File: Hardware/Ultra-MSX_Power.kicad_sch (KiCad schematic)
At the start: 42 parts, among them J1 Conn_KLDX-0202-A, J10 Molex_0469990346, U1 MPU_Z380, U10 SST39SF040, U14 D41464, U15 D41464, U16 D41464, U17 D41464, U3 V9958, U4 YM2610, U5 BQ4802YPW, U6 LMH1980, U8 AS6C4008-55STIN, U9 DAC_YM3016

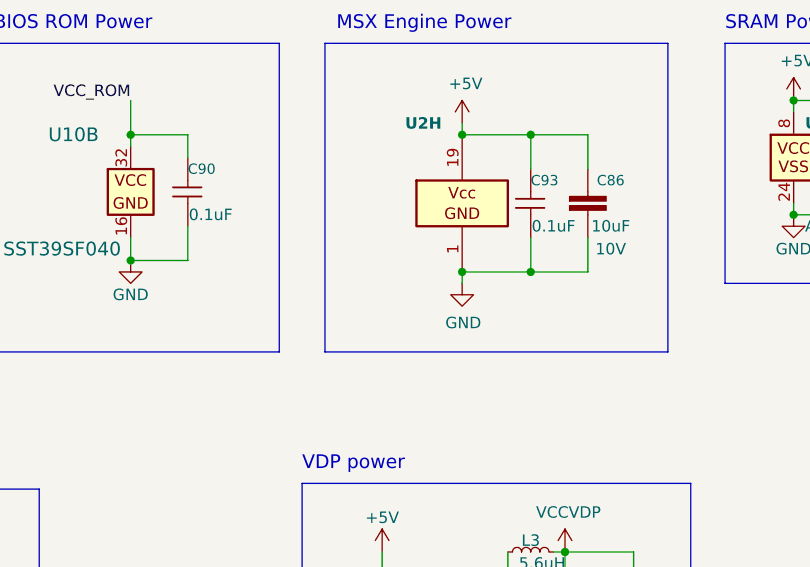
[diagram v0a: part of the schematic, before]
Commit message: Routed the VDP-board further, as well as making it a 4-layer board - also added an exception in the gitignore, for big images.
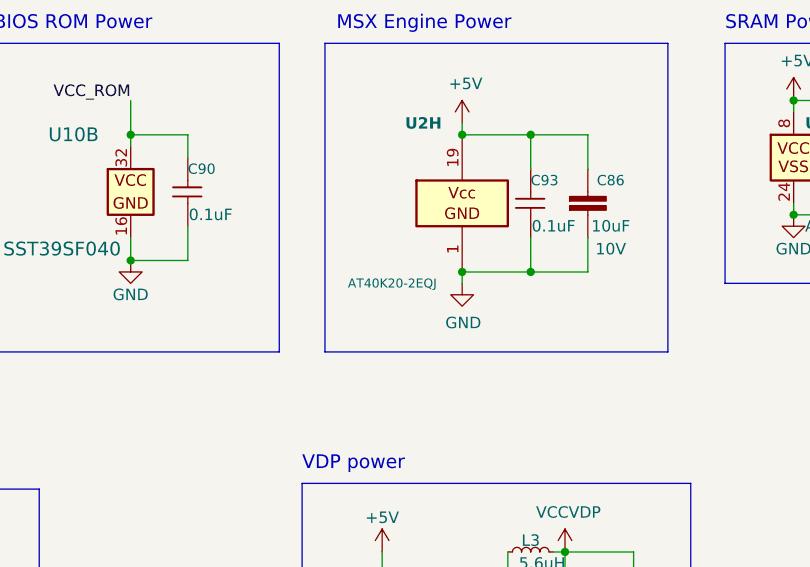
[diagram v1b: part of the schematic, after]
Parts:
- U2: value (none) -> AT40K20-2EQJ; footprint (none) -> Package_QFP:PQFP-240_32.1x32.1mm_P0.5mm
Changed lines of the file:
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@@
       (effects (font (size 1.27 1.27) bold) (justify left))
     )
-    (property "Value" "" (id 1) (at 243.84 53.34 0)
+    (property "Value" "AT40K20-2EQJ" (id 1) (at 243.84 53.34 0)
       (effects (font (size 1 1)) (justify left))
     )
-    (property "Footprint" "" (id 2) (at 290.83 21.59 0)
+    (property "Footprint" "Package_QFP:PQFP-240_32.1x32.1mm_P0.5mm" (id 2) (at 290.83 21.59 0)
       (effects (font (size 1.27 1.27)) (justify left) hide)
     )

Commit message: Finished the VDP-board, finished up the mixer-section, removed the buffer-pins from the FPGA, and instead added external buffers for the slots, designed a marquee-block with the Ultra-MSX logo, designed the logotype, andmultiple other changes.
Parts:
- removed C73, C89: C_GRM21BR71A106KA73K, Capacitor_SMD:C_0805_2012Metric_Pad1.18x1.45mm_HandSolder, symbol LRJ-parts:C_GRM21BR71A106KA73K
- removed C77, C91, C92: C_CC0805JPX7R9BB104, Capacitor_SMD:C_0805_2012Metric, symbol LRJ-parts:C_CC0805JPX7R9BB104
- removed U14, U15, U16, U17: D41464, Ultra-MSX:IC_DIP18_300, symbol Ultra-MSX:D41464
- removed U3: V9958, Ultra-MSX:IC_SDIP64_600, symbol Ultra-MSX:V9958
- removed U6: LMH1980, Package_SO:VSSOP-10_3x3mm_P0.5mm, symbol LRJ-parts:LMH1980
- added C1, C10, C13, C3, C36, C41, C5, C6, C74, C9: C_CC0805JPX7R9BB104, Capacitor_SMD:C_0805_2012Metric, symbol LRJ-parts:C_CC0805JPX7R9BB104
- added C11, C12, C2, C37, C4, C66, C67, C7, C75, C8: C_GRM21BR71A106KA73K, Capacitor_SMD:C_0805_2012Metric_Pad1.18x1.45mm_HandSolder, symbol LRJ-parts:C_GRM21BR71A106KA73K
- added C68, C69: C_GRM32EC81C476KE15K, Capacitor_SMD:C_1210_3225Metric, symbol LRJ-parts:C_GRM32EC81C476KE15K
- added RV1: CAT5140ZI-50, Package_SO:TSSOP-8_3x3mm_P0.65mm, symbol LRJ-parts:CAT5140ZI-50
- added RV4, RV8: AD5144ABRUZ100, Package_SO:TSSOP-20_4.4x6.5mm_P0.65mm, symbol LRJ-parts:AD5144ABRUZ100
- added RV5, RV6: MCP4461, Package_SO:TSSOP-20_4.4x6.5mm_P0.65mm, symbol LRJ-parts:MCP4461
- added U14: SN74ABTH16244DL, Package_SO:TSSOP-56_6.1x14mm_P0.5mm, symbol LRJ-parts:SN74ABTH16244DL
- added U15: SN74ABT241APW, Package_SO:TSSOP-56_6.1x14mm_P0.5mm, symbol LRJ-parts:SN74ABT241APW
- added U6: 74ABT245PW_118, Package_SO:TSSOP-20_4.4x6.5mm_P0.65mm, symbol LRJ-parts:74ABT245PW_118
- added virt_sym1: Virtual_symbol, LRJ:TestPoint_Bridge_Pitch1.5mm_Pad0.8mm, symbol LRJ-parts:Virtual_symbol
- renumbered C17 to C20, J10 to J10-0, J1 to J10-1
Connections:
- net +12V: now also L2.1
- net +5V: now also C1.1, C10.1, C11.1, C12.1, C2.1, C3.1, C4.1, C68.2, C69.2, C74.1, C75.1, C9.1, RV4.17 (V_{LOGIC}), RV8.17 (V_{LOGIC}), U14.18 (VCC), U14.31 (VCC), U14.42 (VCC), U14.7 (VCC), U15.20 (VCC), U6.20 (VCC); no longer L2.1, L3.1
- net +5VSB: now also virt_sym1.1
- net -12V: now also L3.1
- net GND: now also C1.2, C10.2, C11.2, C12.2, C2.2, C3.2, C4.2, C74.2, C75.2, C9.2, RV4.2 (GND), RV8.2 (GND), U14.10 (GND), U14.15 (GND), U14.21 (GND), U14.28 (GND), U14.34 (GND), U14.39 (GND), U14.4 (GND), U14.45 (GND), U15.10 (GND), U6.10 (GND); no longer C28.2, C30.2, C32.1, C33.1, C34.1, C39.1, J10-0.15 (GND), J10-0.17 (GND), J10-0.18 (GND), J10-0.19 (GND), J10-0.24 (GND), J10-0.3 (GND), J10-0.5 (GND), J10-0.7 (GND), J10-1.2, J10-1.3
- net GNDA: now also C13.2, C36.2, C37.2, C41.2, C5.2, C6.2, C66.2, C67.2, C7.2, C8.2, RV1.4 (GND), RV4.9 (V_{SS}), RV5.7 (V_{SS}), RV6.7 (V_{SS}), RV8.9 (V_{SS})
- net VCCRGB: no longer L2.2
- net VCCVDP: no longer L3.2
- net VCC_DAC: now also C13.1, C36.1, C37.1, C41.1, C5.1, C6.1, C66.1, C67.1, C7.1, C8.1, RV1.8 (V_{CC}), RV4.16 (V_{DD}), RV5.17 (V_{DD}), RV6.17 (V_{DD}), RV8.16 (V_{DD})
- net at U1.42 (~{STNBY}): now also virt_sym1.1
- new net +12VA: L2.2
- new net -12VA: L3.2
- new net GNDPWR1: C28.2, C30.2, C32.1, C33.1, C34.1, C39.1, J10-0.15 (GND), J10-0.17 (GND), J10-0.18 (GND), J10-0.19 (GND), J10-0.24 (GND), J10-0.3 (GND), J10-0.5 (GND), J10-0.7 (GND)
- new net GNDPWR2: C68.1, C69.1, J10-1.2, J10-1.3
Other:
- note added: "ATX connector"
- note added: "Barreljack Backup"
- note added: "Digital Potentiometer power"
- note added: "Filtering for analogue components"
- note added: "Power-management: ---- https://www.embedded.com/adding-a-power-management-mcu-to-your-system-reduces-standby-energy-use/ -- MAKE A STAR-GROUND-CONNECTION!"
- note added: "Primary Power input"
- note added: "Slot Buffer Power"
- note removed: "Power-management: ---- https://www.embedded.com/adding-a-power-management-mcu-to-your-system-reduces-standby-energy-use/"
- note removed: "Primary Power input (ATX)"
- note removed: "Sync Separator power"
- note removed: "VDP power"
- note removed: "VRAM Power"
- note removed: "https://powersupply33.com/atx-power-supply-pinout.html https://pinouts.ru/Power/atx_v2_pinout.shtml"
- moved on the sheet: C15, C16, C22, C28, C30, C32, C33, C34, C39, C59, C63, C86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

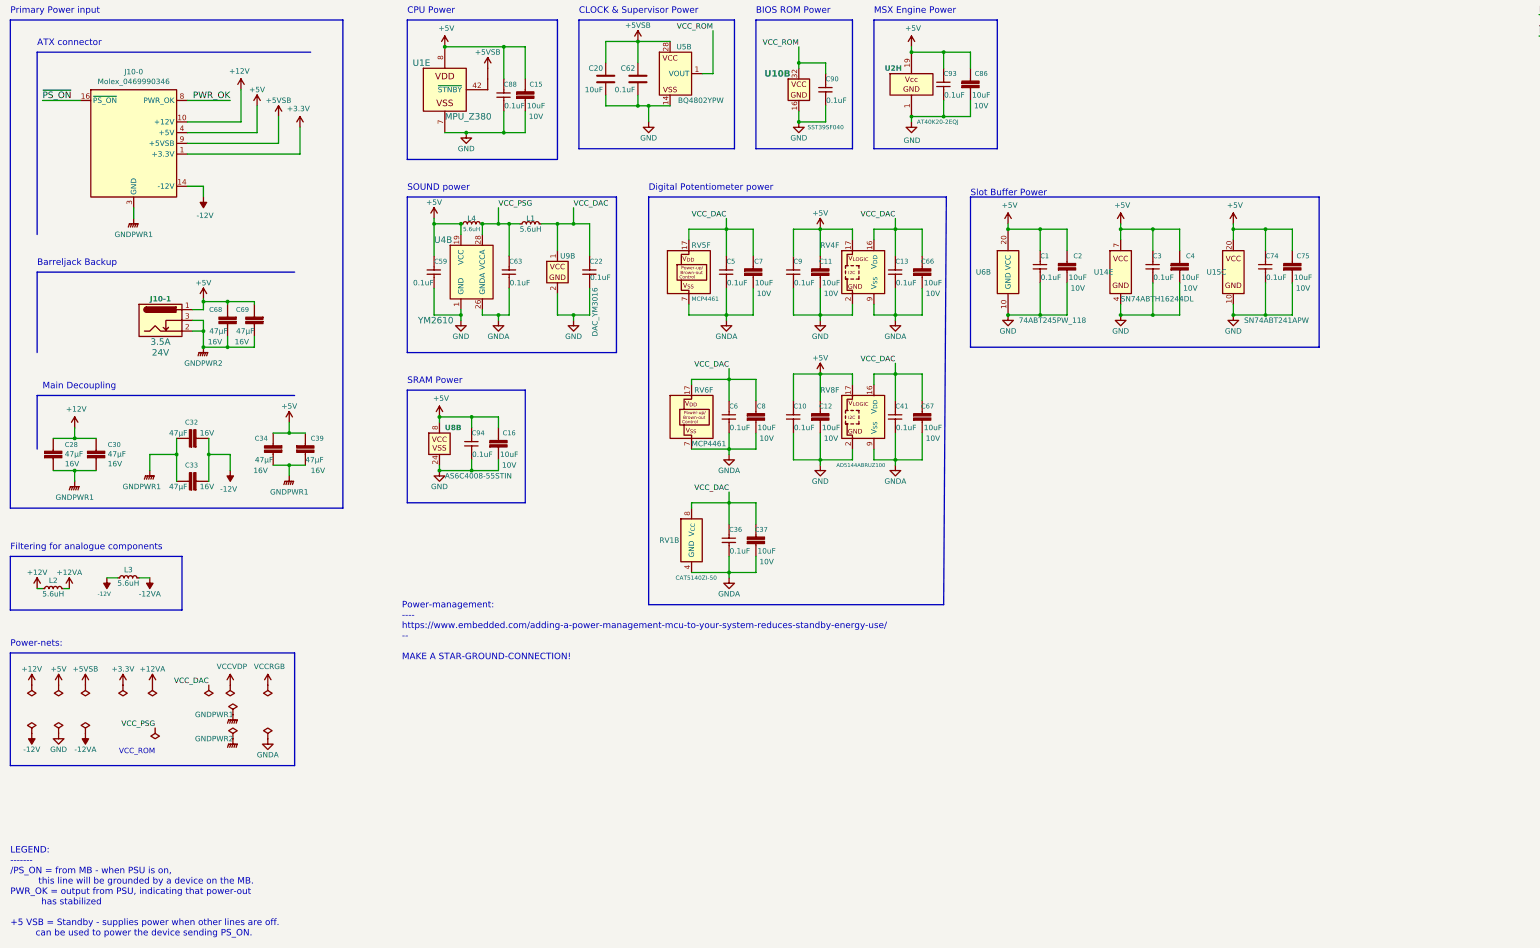
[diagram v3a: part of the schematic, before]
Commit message: Added SD-card slot, made basic 3d-model for sd-card slot, connected it up in the schematic, and numerous other tweaks.
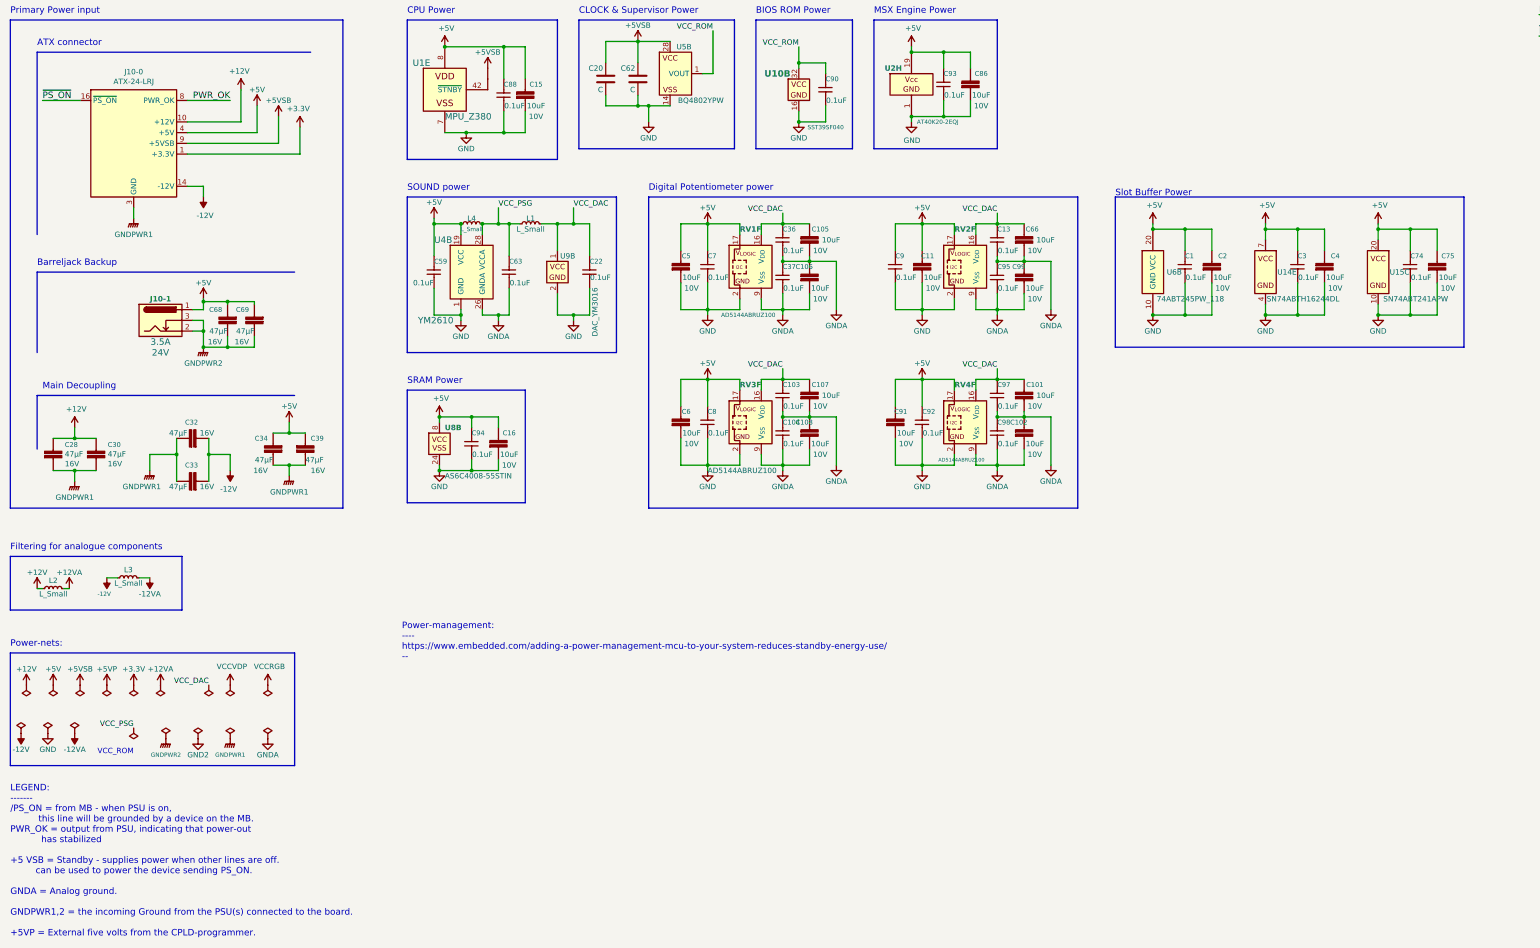
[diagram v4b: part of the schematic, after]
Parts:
- removed C10, C41, C5, C6: C_CC0805JPX7R9BB104, Capacitor_SMD:C_0805_2012Metric, symbol LRJ-parts:C_CC0805JPX7R9BB104
- removed C12, C37, C67, C7, C8: C_GRM21BR71A106KA73K, Capacitor_SMD:C_0805_2012Metric_Pad1.18x1.45mm_HandSolder, symbol LRJ-parts:C_GRM21BR71A106KA73K
- removed RV1: CAT5140ZI-50, Package_SO:TSSOP-8_3x3mm_P0.65mm, symbol LRJ-parts:CAT5140ZI-50
- removed RV8: AD5144ABRUZ100, Package_SO:TSSOP-20_4.4x6.5mm_P0.65mm, symbol LRJ-parts:AD5144ABRUZ100
- added C101, C102, C105, C106, C107, C108, C5, C6, C91, C99: C_GRM21BR71A106KA73K, Capacitor_SMD:C_0805_2012Metric_Pad1.18x1.45mm_HandSolder, symbol LRJ-parts:C_GRM21BR71A106KA73K
- added C103, C104, C37, C7, C8, C92, C95, C97, C98: C_CC0805JPX7R9BB104, Capacitor_SMD:C_0805_2012Metric, symbol LRJ-parts:C_CC0805JPX7R9BB104
- added RV4: AD5144ABRUZ100, Package_SO:TSSOP-20_4.4x6.5mm_P0.65mm, symbol LRJ-parts:AD5144ABRUZ100
- C20: value 10uF -> C
- C62: value 0.1uF -> C
- J10-0: value Molex_0469990346 -> ATX-24-LRJ
- L1, L2, L3, L4: value 5.6uH -> L_Small
- RV1: renamed from RV5; value MCP4461 -> AD5144ABRUZ100; symbol LRJ-parts:MCP4461 -> LRJ-parts:AD5144ABRUZ100; MPN MCP4461-503E/ST -> AD5144ABRUZ100; Manufacturer Microchip Technology -> Analog Devices Inc.; Tolerance (none) -> ±8%
- RV2: renamed from RV4; Tolerance (none) -> ±8%
- RV3: renamed from RV6; value MCP4461 -> AD5144ABRUZ100; symbol LRJ-parts:MCP4461 -> LRJ-parts:AD5144ABRUZ100; MPN MCP4461-503E/ST -> AD5144ABRUZ100; Manufacturer Microchip Technology -> Analog Devices Inc.; Tolerance (none) -> ±8%
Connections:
- net +5V: now also RV1.17 (V_{LOGIC}), RV3.17 (V_{LOGIC}), C5.1, C6.1, C7.1, C8.1, C91.1, C92.1, RV4.17 (V_{LOGIC})
- net GND: now also RV1.2 (GND), RV3.2 (GND), C5.2, C6.2, C7.2, C8.2, C91.2, C92.2, RV4.2 (GND)
- net GNDA: now also RV1.9 (V_{SS}), RV3.9 (V_{SS}), C101.2, C102.1, C102.2, C103.2, C104.1, C104.2, C105.2, C106.1, C106.2, C107.2, C108.1, C108.2, C37.1, C37.2, C95.1, C95.2, C97.2, C98.1, C98.2, C99.1, C99.2, RV4.9 (V_{SS}); no longer RV1.7 (V_{SS}), RV3.7 (V_{SS})
- net VCC_DAC: now also RV1.16 (V_{DD}), RV3.16 (V_{DD}), C101.1, C103.1, C105.1, C107.1, C97.1, RV4.16 (V_{DD}); no longer RV1.17 (V_{DD}), RV3.17 (V_{DD})
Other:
- note added: "LEGEND: ------- /PS_ON = from MB - when PSU is on, this line will be grounded by a device on the MB. PWR_OK = output from PSU, indicating that power-out has stabilized +5 VSB = Standby - supplies power when other lines are off. can be used to power the device sending PS_ON. GNDA = Analog ground. GNDPWR1,2 = the incoming Ground from the PSU(s) connected to the board. +5VP = External five volts fro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"
- note added: "Power-management: ---- https://www.embedded.com/adding-a-power-management-mcu-to-your-system-reduces-standby-energy-use/ --"
- note removed: "LEGEND: ------- /PS_ON = from MB - when PSU is on, this line will be grounded by a device on the MB. PWR_OK = output from PSU, indicating that power-out has stabilized +5 VSB = Standby - supplies power when other lines are off. can be used to power the device sending PS_ON."
- note removed: "Power-management: ---- https://www.embedded.com/adding-a-power-management-mcu-to-your-system-reduces-standby-energy-use/ -- MAKE A STAR-GROUND-CONNECTION!"
- moved on the sheet: C1, C11, C13, C2, C3, C4, C66, C74, C75, C9, RV2F

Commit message: Redesigned VDP-board to include a socket, increased it to 4 layers. Various clean-ups here and there. Improved the printer-port and joystick-port 3D-models. Improved the cooling-fin 3D-model, and added attachment-spring in 3D-model.
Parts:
- U14: footprint Package_SO:TSSOP-56_6.1x14mm_P0.5mm -> LRJ:Texas_R-PDSO-G48_7.7x16.0mm
- U15: footprint Package_SO:TSSOP-56_6.1x14mm_P0.5mm -> Package_SO:Texas_PWP0020A; MPN SN74ABTH16244DL -> SN74ABT241APW
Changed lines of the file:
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@@
     (property "Reference" "U15" (id 0) (at 347.98 85.09 0))
     (property "Value" "SN74ABT241APW" (id 1) (at 351.79 91.44 0))
-    (property "Footprint" "Package_SO:TSSOP-56_6.1x14mm_P0.5mm" (id 2) (at 304.8 77.47 0)
+    (property "Footprint" "Package_SO:Texas_PWP0020A" (id 2) (at 304.8 77.47 0)
       (effects (font (size 1.27 1.27)) hide)
     )
@@
       (effects (font (size 1.27 1.27)) hide)
     )
-    (property "MPN" "SN74ABTH16244DL" (id 5) (at 314.96 67.31 0)
-      (effects (font (size 1.27 1.27)) hide)
-    )
-    (property "Description" "BUF NON-INVERT 5.5V 48SSOP" (id 6) (at 309.88 72.39 0)
+    (property "MPN" "SN74ABT241APW" (id 5) (at 314.96 67.31 0)
+      (effects (font (size 1.27 1.27)) hide)
+    )
+    (property "Description" "BUF NON-INVERT 5.5V 20-TSSOP" (id 6) (at 309.88 72.39 0)
       (effects (font (size 1.27 1.27)) hide)
     )
@@
     (property "Reference" "U14" (id 0) (at 321.31 85.09 0))
     (property "Value" "SN74ABTH16244DL" (id 1) (at 325.12 91.44 0))
-    (property "Footprint" "Package_SO:TSSOP-56_6.1x14mm_P0.5mm" (id 2) (at 278.13 77.47 0)
-      (effects (font (size 1.27 1.27)) hide)
-    )
+    (property "Footprint" "LRJ:Texas_R-PDSO-G48_7.7x16.0mm" (id 2) (at 278.13 77.47 0)
+      (effects (font (size 1.27 1.27)) hide)
+    )

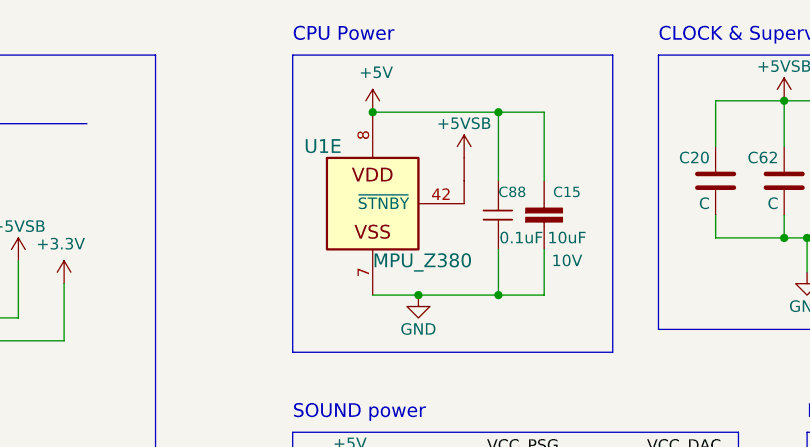
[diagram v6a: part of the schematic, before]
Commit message: Reworked the Printer-port 3D model, and the Scart 3D-model. Generated a 3D model of the main board. Moved peripheral components from separate expansion-headers, to a singular IO-shield board.
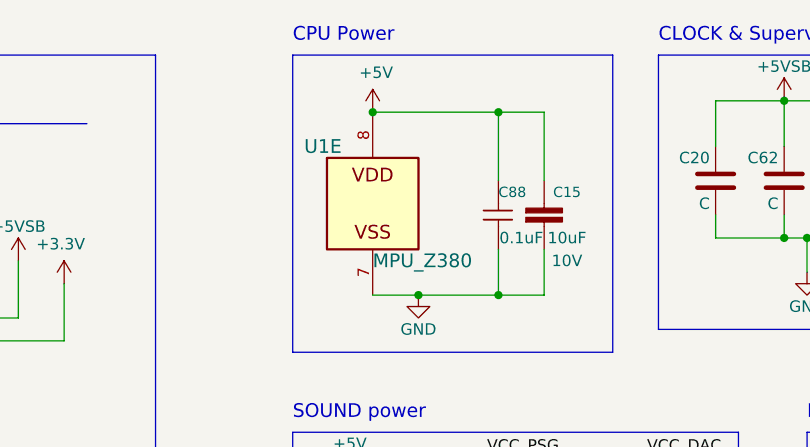
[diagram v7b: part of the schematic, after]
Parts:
- removed virt_sym1: Virtual_symbol, LRJ:TestPoint_Bridge_Pitch1.5mm_Pad0.8mm, symbol LRJ-parts:Virtual_symbol
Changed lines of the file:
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@@
     (pin "40")
     (pin "41")
+    (pin "42")
     (pin "43")
     (pin "11")
@@
     (pin "29")
     (pin "30")
-    (pin "42")
     (pin "50")
     (pin "51")
@@
     (pin "2")
   )
-  (symbol (lib_id "LRJ-parts:Virtual_symbol") (at 132.08 39.37 0) (unit 1)
-    (in_bom no) (on_board no) (fields_autoplaced)
-    (property "Reference" "virt_sym1" (id 0) (at 137.16 36.83 0)
-      (effects (font (size 1.27 1.27)) hide)
-    )
-    (property "Value" "Virtual_symbol" (id 1) (at 139.7 39.37 0)
-      (effects (font (size 1.27 1.27)) hide)
-    )
-    (property "Footprint" "LRJ:TestPoint_Bridge_Pitch1.5mm_Pad0.8mm" (id 2) (at 132.715 48.26 0)
-      (effects (font (size 1.27 1.27)) hide)
-    )
-    (property "Datasheet" "" (id 3) (at 134.62 36.83 0)
-      (effects (font (size 1.27 1.27)) hide)
-    )
-    (pin "1")
-    (pin "1")
-  )
   (symbol (lib_id "power:GND") (at 289.56 95.25 0) (unit 1)
     (in_bom yes) (on_board yes)
@@
     (pin "7")
   )
-  (symbol (lib_id "LRJ-parts:+5VSB") (at 132.08 36.83 0) (unit 1)
-    (in_bom no) (on_board yes)
-    (property "Reference" "#PWR034" (id 0) (at 132.08 40.64 0)
-      (effects (font (size 1.27 1.27)) hide)
-    )
-    (property "Value" "+5VSB" (id 1) (at 132.08 33.02 0))
-    (property "Footprint" "" (id 2) (at 132.08 36.83 0)
-      (effects (font (size 1.27 1.27)) hide)
-    )
-    (property "Datasheet" "" (id 3) (at 132.08 36.83 0)
-      (effects (font (size 1.27 1.27)) hide)
-    )
-    (property "Description" "Standby-power, 10 mA max (ATX v.1.x) or  2A max (ATX v.2.2+)" (id 4) (at 132.08 46.99 0)
-      (effects (font (size 1.27 1.27)) hide)
-    )
-    (pin "1")
-  )
   (symbol (lib_id "LRJ-parts:GNDPWR1") (at 48.26 72.39 0) (unit 1)
